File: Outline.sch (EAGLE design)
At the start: 51 parts, among them CN1 0675031020, IC1 ATXMEGA32A4U-AU, IC2 ST1480ACDR, J1 RJHSE5080, J2 J2, U1 NCP1117DTAG @ 3.3v, U2 NCP1117DTAG @ 12v

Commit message: 4.2.1
Updated Layout
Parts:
- removed U$6: 10W_RGB_LED, TechIsCool:10W_RGB_LED
- added U$3: 10W_RGB_LED, TechIsCool:10W_RGB_LED
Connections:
- net BLUE_A: now also U$3.B$A; no longer U$6.B$2
- net BLUE_C: now also U$3.B$C; no longer U$6.B$1
- net GREEN_A: now also U$3.G$A; no longer U$6.G$2
- net GREEN_C: now also U$3.G$C; no longer U$6.G$1
- net RED_A: now also U$3.R$A; no longer U$6.R$2
- net RED_C: now also U$3.R$C; no longer U$6.R$1
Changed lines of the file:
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@@
 <grid distance="0.01" unitdist="inch" unit="inch" style="lines" multiple="1" display="no" altdistance="0.01" altunitdist="inch" altunit="inch"/>
 <layers>
-<layer number="1" name="Top" color="4" fill="1" visible="no" active="no"/>
-<layer number="16" name="Bottom" color="1" fill="1" visible="no" active="no"/>
-<layer number="17" name="Pads" color="2" fill="1" visible="no" active="no"/>
-<layer number="18" name="Vias" color="2" fill="1" visible="no" active="no"/>
-<layer number="19" name="Unrouted" color="6" fill="1" visible="no" active="no"/>
-<layer number="20" name="Dimension" color="15" fill="1" visible="no" active="no"/>
-<layer number="21" name="tPlace" color="7" fill="1" visible="no" active="no"/>
-<layer number="22" name="bPlace" color="7" fill="1" visible="no" active="no"/>
-<layer number="23" name="tOrigins" color="15" fill="1" visible="no" active="no"/>
-<layer number="24" name="bOrigins" color="15" fill="1" visible="no" active="no"/>
-<layer number="25" name="tNames" color="7" fill="1" visible="no" active="no"/>
-<layer number="26" name="bNames" color="7" fill="1" visible="no" active="no"/>
-<layer number="27" name="tValues" color="7" fill="1" visible="no" active="no"/>
-<layer number="28" name="bValues" color="7" fill="1" visible="no" active="no"/>
+<layer number="1" name="Top" color="4" fill="1" visible="yes" active="no"/>
+<layer number="16" name="Bottom" color="1" fill="1" visible="yes" active="no"/>
+<layer number="17" name="Pads" color="2" fill="1" visible="yes" active="no"/>
+<layer number="18" name="Vias" color="2" fill="1" visible="yes" active="no"/>
+<layer number="19" name="Unrouted" color="6" fill="1" visible="yes" active="no"/>
+<layer number="20" name="Dimension" color="15" fill="1" visible="yes" active="no"/>
+<layer number="21" name="tPlace" color="7" fill="1" visible="yes" active="no"/>
+<layer number="22" name="bPlace" color="7" fill="1" visible="yes" active="no"/>
+<layer number="23" name="tOrigins" color="15" fill="1" visible="yes" active="no"/>
+<layer number="24" name="bOrigins" color="15" fill="1" visible="yes" active="no"/>
+<layer number="25" name="tNames" color="7" fill="1" visible="yes" active="no"/>
+<layer number="26" name="bNames" color="7" fill="1" visible="yes" active="no"/>
+<layer number="27" name="tValues" color="7" fill="1" visible="yes" active="no"/>
+<layer number="28" name="bValues" color="7" fill="1" visible="yes" active="no"/>
 <layer number="29" name="tStop" color="7" fill="3" visible="no" active="no"/>
 <layer number="30" name="bStop" color="7" fill="6" visible="no" active="no"/>
@@
 <layer number="35" name="tGlue" color="7" fill="4" visible="no" active="no"/>
 <layer number="36" name="bGlue" color="7" fill="5" visible="no" active="no"/>
-<layer number="37" name="tTest" color="7" fill="1" visible="no" active="no"/>
-<layer number="38" name="bTest" color="7" fill="1" visible="no" active="no"/>
+<layer number="37" name="tTest" color="7" fill="1" visible="yes" active="no"/>
+<layer number="38" name="bTest" color="7" fill="1" visible="yes" active="no"/>
 <layer number="39" name="tKeepout" color="4" fill="11" visible="no" active="no"/>
 <layer number="40" name="bKeepout" color="1" fill="11" visible="no" active="no"/>
@@
 <layer number="44" name="Drills" color="7" fill="1" visible="no" active="no"/>
 <layer number="45" name="Holes" color="7" fill="1" visible="no" active="no"/>
-<layer number="46" name="Milling" color="3" fill="1" visible="no" active="no"/>
-<layer number="47" name="Measures" color="7" fill="1" visible="no" active="no"/>
-<layer number="48" name="Document" color="7" fill="1" visible="no" active="no"/>
-<layer number="49" name="Reference" color="7" fill="1" visible="no" active="no"/>
-<layer number="50" name="dxf" color="7" fill="1" visible="no" active="no"/>
-<layer number="51" name="tDocu" color="7" fill="1" visible="no" active="no"/>
-<layer number="52" name="bDocu" color="7" fill="1" visible="no" active="no"/>
-<layer number="53" name="tGND_GNDA" color="7" fill="9" visible="no" active="no"/>
-<layer number="54" name="bGND_GNDA" color="1" fill="9" visible="no" active="no"/>
-<layer number="56" name="wert" color="7" fill="1" visible="no" active="no"/>
+<layer number="46" name="Milling" color="3" fill="1" visible="yes" active="no"/>
+<layer number="47" name="Measures" color="7" fill="1" visible="yes" active="no"/>
+<layer number="48" name="Document" color="7" fill="1" visible="yes" active="no"/>
+<layer number="49" name="Reference" color="7" fill="1" visible="yes" active="no"/>
+<layer number="50" name="dxf" color="7" fill="1" visible="yes" active="no"/>
+<layer number="51" name="tDocu" color="7" fill="1" visible="yes" active="no"/>
+<layer number="52" name="bDocu" color="7" fill="1" visible="yes" active="no"/>
+<layer number="53" name="tGND_GNDA" color="7" fill="9" visible="yes" active="no"/>
+<layer number="54" name="bGND_GNDA" color="1" fill="9" visible="yes" active="no"/>
+<layer number="56" name="wert" color="7" fill="1" visible="yes" active="no"/>
 <layer number="91" name="Nets" color="2" fill="1" visible="yes" active="yes"/>
 <layer number="92" name="Busses" color="1" fill="1" visible="yes" active="yes"/>
@@
 <part name="C14" library="SparkFun" deviceset="CAP" device="0603-CAP" value=".1uF"/>
 <part name="FRAME1" library="frames" deviceset="DINA4_L" device=""/>
-<part name="U$6" library="TechIsCool" deviceset="10W_RGB_LED" device=""/>
 <part name="GND20" library="supply1" deviceset="GND" device=""/>
 <part name="U$2" library="TechIsCool" deviceset="DS18B20" device=""/>
@@
 <part name="R6" library="nonolith" deviceset="RESISTOR" device="0603" value="1k Ohm"/>
 <part name="SC_D3" library="TechIsCool" deviceset="SCHOTTKY_2" device="" value="1PS74SB23"/>
+<part name="U$3" library="TechIsCool" deviceset="10W_RGB_LED" device=""/>
 </parts>
 <sheets>
@@
 <instance part="FRAME1" gate="G$1" x="0.254" y="0"/>
 <instance part="FRAME1" gate="G$2" x="162.814" y="0"/>
-<instance part="U$6" gate="G$1" x="34.798" y="171.45"/>
 <instance part="GND20" gate="1" x="122.174" y="23.114" rot="R90"/>
 <instance part="U$2" gate="G$1" x="26.162" y="21.336"/>
@@
 <instance part="R6" gate="G$1" x="101.092" y="157.48"/>
 <instance part="SC_D3" gate="G$1" x="190.5" y="62.484" rot="R270"/>
+<instance part="U$3" gate="1" x="35.56" y="168.148"/>
 </instances>
 <busses>
@@
 <net name="RED_A" class="0">
 <segment>
-<pinref part="U$6" gate="G$1" pin="R$2"/>
 <wire x1="28.448" y1="171.45" x2="20.828" y2="171.45" width="0.1524" layer="91"/>
 <label x="19.558" y="171.704" size="1.778" layer="95"/>
+<pinref part="U$3" gate="1" pin="R$A"/>
 </segment>
 <segment>
@@
 <net name="GREEN_A" class="0">
 <segment>
-<pinref part="U$6" gate="G$1" pin="G$2"/>
 <wire x1="28.448" y1="168.148" x2="20.828" y2="168.148" width="0.1524" layer="91"/>
 <label x="15.748" y="168.402" size="1.778" layer="95"/>
+<pinref part="U$3" gate="1" pin="G$A"/>
 </segment>
 <segment>
@@
 <net name="BLUE_A" class="0">
 <segment>
-<pinref part="U$6" gate="G$1" pin="B$2"/>
 <wire x1="28.448" y1="164.846" x2="20.828" y2="164.846" width="0.1524" layer="91"/>
 <label x="18.034" y="165.1" size="1.778" layer="95"/>
+<pinref part="U$3" gate="1" pin="B$A"/>
 </segment>
 <segment>
@@
 <net name="RED_C" class="0">
 <segment>
-<pinref part="U$6" gate="G$1" pin="R$1"/>
 <wire x1="41.148" y1="171.45" x2="49.276" y2="171.45" width="0.1524" layer="91"/>
 <label x="41.402" y="171.704" size="1.778" layer="95"/>
+<pinref part="U$3" gate="1" pin="R$C"/>
 </segment>
 <segment>
@@
 <net name="GREEN_C" class="0">
 <segment>
-<pinref part="U$6" gate="G$1" pin="G$1"/>
 <wire x1="41.148" y1="168.148" x2="49.276" y2="168.148" width="0.1524" layer="91"/>
 <label x="41.402" y="168.402" size="1.778" layer="95"/>
+<pinref part="U$3" gate="1" pin="G$C"/>
 </segment>
 <segment>
@@
 <net name="BLUE_C" class="0">
 <segment>
-<pinref part="U$6" gate="G$1" pin="B$1"/>
 <wire x1="41.148" y1="164.846" x2="49.276" y2="164.846" width="0.1524" layer="91"/>
 <label x="41.402" y="165.1" size="1.778" layer="95"/>
-</segment>
-<segment>
+<pinref part="U$3" gate="1" pin="B$C"/>
+</segment>
+<segment>

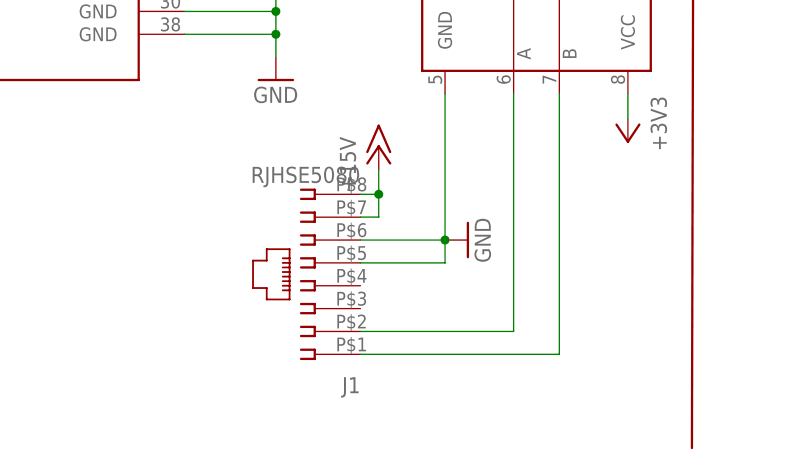
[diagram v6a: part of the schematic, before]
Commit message: 4.2.2
Connected a few things and add a via. Also gnded the extra wires in the
RJ45 cable
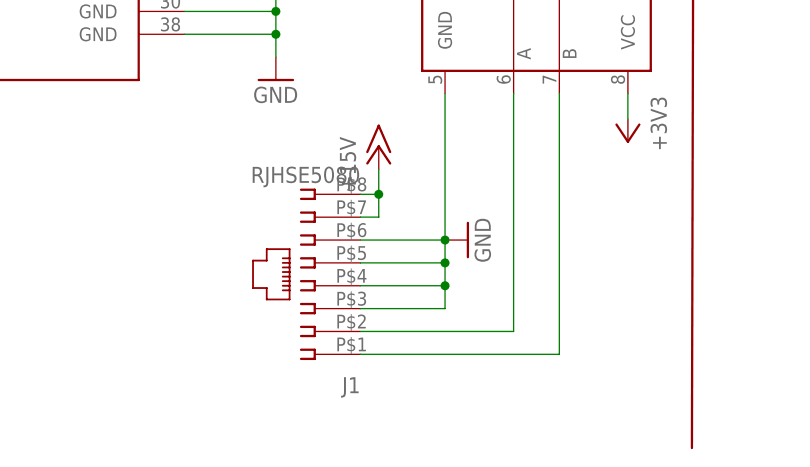
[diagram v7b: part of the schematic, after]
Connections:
- net GND: now also J1.3, J1.4
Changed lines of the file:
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@@
 <grid distance="0.01" unitdist="inch" unit="inch" style="lines" multiple="1" display="no" altdistance="0.01" altunitdist="inch" altunit="inch"/>
 <layers>
-<layer number="1" name="Top" color="4" fill="1" visible="yes" active="no"/>
-<layer number="16" name="Bottom" color="1" fill="1" visible="yes" active="no"/>
-<layer number="17" name="Pads" color="2" fill="1" visible="yes" active="no"/>
-<layer number="18" name="Vias" color="2" fill="1" visible="yes" active="no"/>
-<layer number="19" name="Unrouted" color="6" fill="1" visible="yes" active="no"/>
-<layer number="20" name="Dimension" color="15" fill="1" visible="yes" active="no"/>
-<layer number="21" name="tPlace" color="7" fill="1" visible="yes" active="no"/>
-<layer number="22" name="bPlace" color="7" fill="1" visible="yes" active="no"/>
-<layer number="23" name="tOrigins" color="15" fill="1" visible="yes" active="no"/>
-<layer number="24" name="bOrigins" color="15" fill="1" visible="yes" active="no"/>
-<layer number="25" name="tNames" color="7" fill="1" visible="yes" active="no"/>
-<layer number="26" name="bNames" color="7" fill="1" visible="yes" active="no"/>
-<layer number="27" name="tValues" color="7" fill="1" visible="yes" active="no"/>
-<layer number="28" name="bValues" color="7" fill="1" visible="yes" active="no"/>
+<layer number="1" name="Top" color="4" fill="1" visible="no" active="no"/>
+<layer number="16" name="Bottom" color="1" fill="1" visible="no" active="no"/>
+<layer number="17" name="Pads" color="2" fill="1" visible="no" active="no"/>
+<layer number="18" name="Vias" color="2" fill="1" visible="no" active="no"/>
+<layer number="19" name="Unrouted" color="6" fill="1" visible="no" active="no"/>
+<layer number="20" name="Dimension" color="15" fill="1" visible="no" active="no"/>
+<layer number="21" name="tPlace" color="7" fill="1" visible="no" active="no"/>
+<layer number="22" name="bPlace" color="7" fill="1" visible="no" active="no"/>
+<layer number="23" name="tOrigins" color="15" fill="1" visible="no" active="no"/>
+<layer number="24" name="bOrigins" color="15" fill="1" visible="no" active="no"/>
+<layer number="25" name="tNames" color="7" fill="1" visible="no" active="no"/>
+<layer number="26" name="bNames" color="7" fill="1" visible="no" active="no"/>
+<layer number="27" name="tValues" color="7" fill="1" visible="no" active="no"/>
+<layer number="28" name="bValues" color="7" fill="1" visible="no" active="no"/>
 <layer number="29" name="tStop" color="7" fill="3" visible="no" active="no"/>
 <layer number="30" name="bStop" color="7" fill="6" visible="no" active="no"/>
@@
 <layer number="35" name="tGlue" color="7" fill="4" visible="no" active="no"/>
 <layer number="36" name="bGlue" color="7" fill="5" visible="no" active="no"/>
-<layer number="37" name="tTest" color="7" fill="1" visible="yes" active="no"/>
-<layer number="38" name="bTest" color="7" fill="1" visible="yes" active="no"/>
+<layer number="37" name="tTest" color="7" fill="1" visible="no" active="no"/>
+<layer number="38" name="bTest" color="7" fill="1" visible="no" active="no"/>
 <layer number="39" name="tKeepout" color="4" fill="11" visible="no" active="no"/>
 <layer number="40" name="bKeepout" color="1" fill="11" visible="no" active="no"/>
@@
 <layer number="44" name="Drills" color="7" fill="1" visible="no" active="no"/>
 <layer number="45" name="Holes" color="7" fill="1" visible="no" active="no"/>
-<layer number="46" name="Milling" color="3" fill="1" visible="yes" active="no"/>
-<layer number="47" name="Measures" color="7" fill="1" visible="yes" active="no"/>
-<layer number="48" name="Document" color="7" fill="1" visible="yes" active="no"/>
-<layer number="49" name="Reference" color="7" fill="1" visible="yes" active="no"/>
-<layer number="50" name="dxf" color="7" fill="1" visible="yes" active="no"/>
-<layer number="51" name="tDocu" color="7" fill="1" visible="yes" active="no"/>
-<layer number="52" name="bDocu" color="7" fill="1" visible="yes" active="no"/>
-<layer number="53" name="tGND_GNDA" color="7" fill="9" visible="yes" active="no"/>
-<layer number="54" name="bGND_GNDA" color="1" fill="9" visible="yes" active="no"/>
-<layer number="56" name="wert" color="7" fill="1" visible="yes" active="no"/>
+<layer number="46" name="Milling" color="3" fill="1" visible="no" active="no"/>
+<layer number="47" name="Measures" color="7" fill="1" visible="no" active="no"/>
+<layer number="48" name="Document" color="7" fill="1" visible="no" active="no"/>
+<layer number="49" name="Reference" color="7" fill="1" visible="no" active="no"/>
+<layer number="50" name="dxf" color="7" fill="1" visible="no" active="no"/>
+<layer number="51" name="tDocu" color="7" fill="1" visible="no" active="no"/>
+<layer number="52" name="bDocu" color="7" fill="1" visible="no" active="no"/>
+<layer number="53" name="tGND_GNDA" color="7" fill="9" visible="no" active="no"/>
+<layer number="54" name="bGND_GNDA" color="1" fill="9" visible="no" active="no"/>
+<layer number="56" name="wert" color="7" fill="1" visible="no" active="no"/>
 <layer number="91" name="Nets" color="2" fill="1" visible="yes" active="yes"/>
 <layer number="92" name="Busses" color="1" fill="1" visible="yes" active="yes"/>
@@
 <wire x1="119.634" y1="20.574" x2="110.236" y2="20.574" width="0.1524" layer="91"/>
 <junction x="119.634" y="23.114"/>
-</segment>
-<segment>
+<pinref part="J1" gate="G$1" pin="4"/>
+<wire x1="110.236" y1="18.034" x2="119.634" y2="18.034" width="0.1524" layer="91"/>
+<wire x1="119.634" y1="18.034" x2="119.634" y2="20.574" width="0.1524" layer="91"/>
+<pinref part="J1" gate="G$1" pin="3"/>
+<wire x1="110.236" y1="15.494" x2="119.634" y2="15.494" width="0.1524" layer="91"/>
+<wire x1="119.634" y1="15.494" x2="119.634" y2="18.034" width="0.1524" layer="91"/>
+<junction x="119.634" y="20.574"/>
+<junction x="119.634" y="18.034"/>
+</segment>
+<segment>
